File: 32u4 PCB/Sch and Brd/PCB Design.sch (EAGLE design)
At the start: 53 parts, among them J1 AVR_SPI_PROG_3X2PTH, J2 AMP FCI 10103594-0001LF, Q1 16MHz, U1 ATMEGA32U4-AU

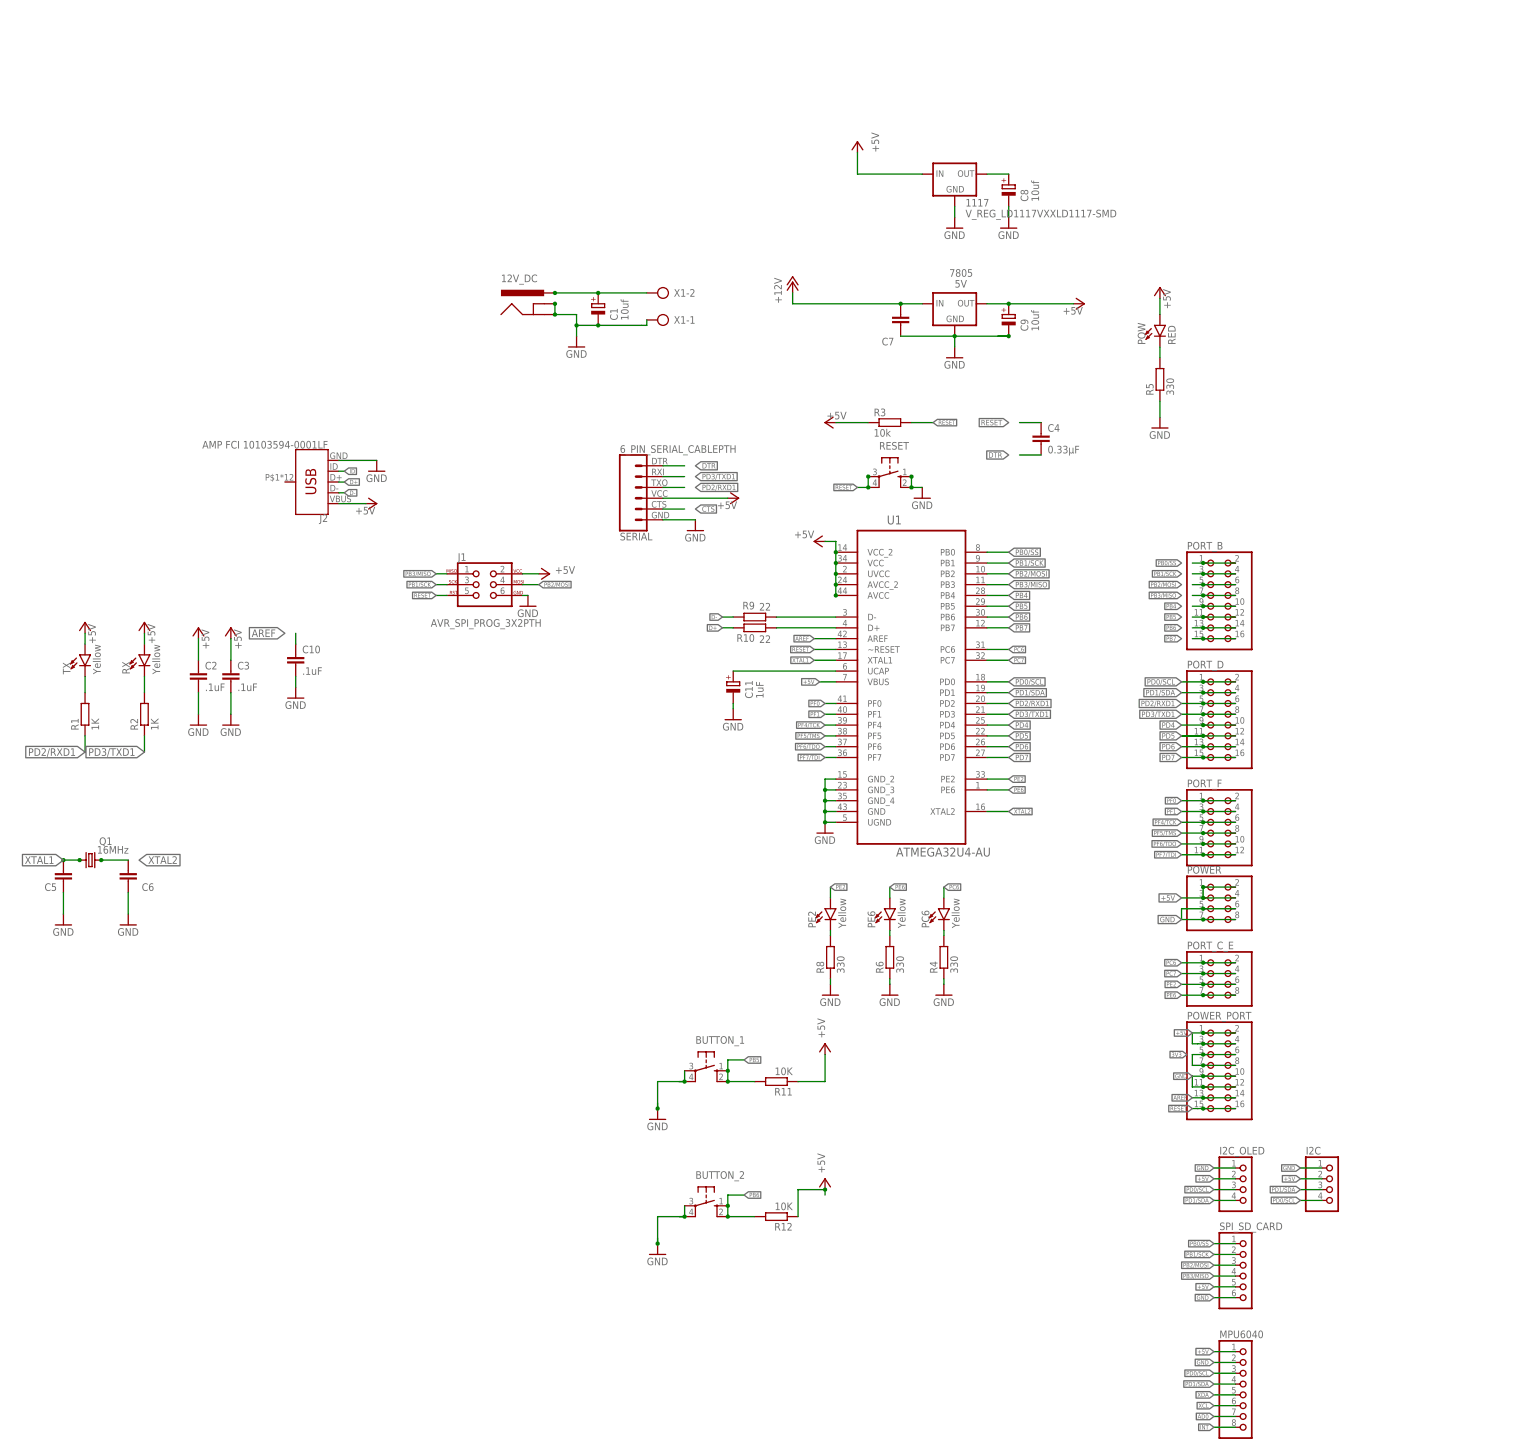
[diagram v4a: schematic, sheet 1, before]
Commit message: Adjusted Silkscreen, added bluetooth
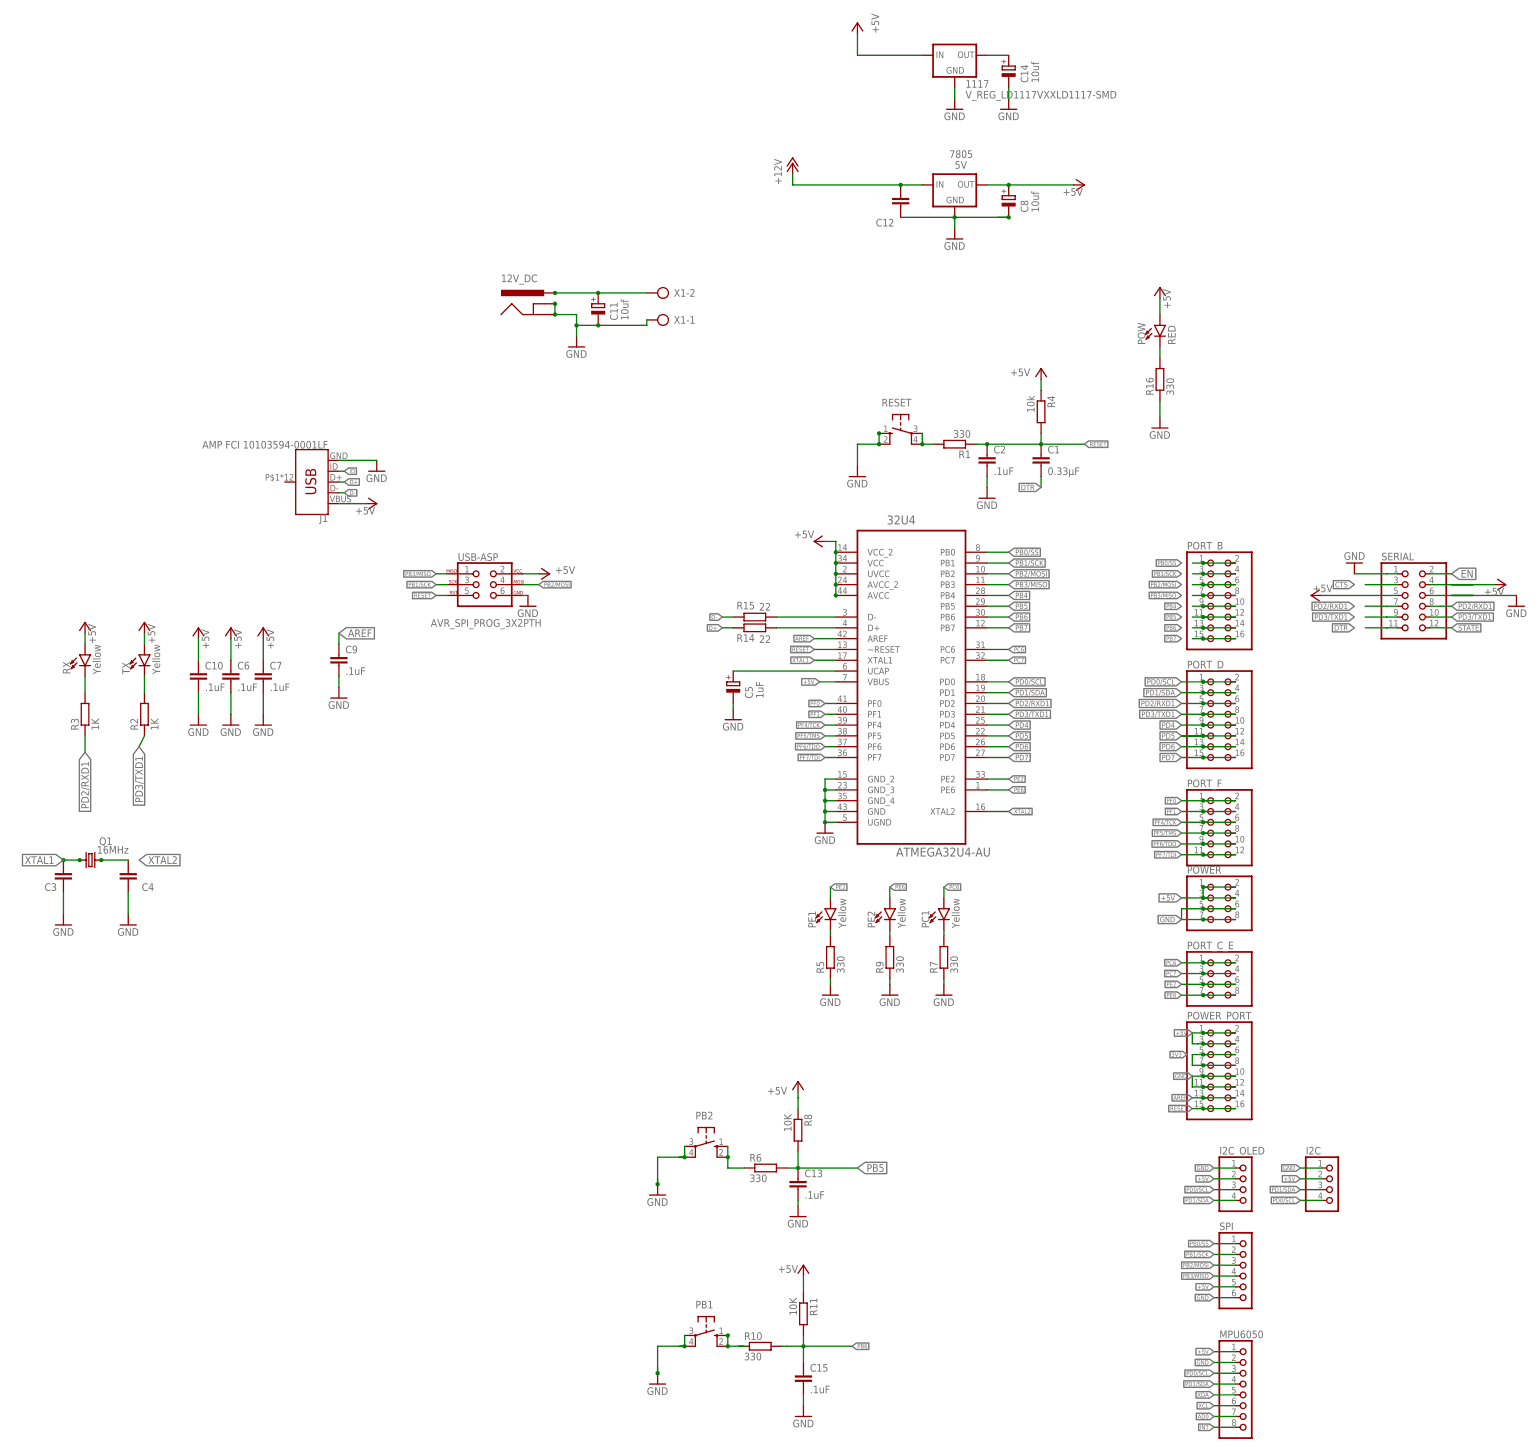
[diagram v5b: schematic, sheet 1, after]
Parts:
- removed BUTTON_1, BUTTON_2: (no value), switch-omron:10-XX
- removed J2: AMP FCI 10103594-0001LF, SparkFun-Connectors:USB_MICRO-B_HALF_PTH
- removed PE6: Yellow, SparkFun-LED:LED-BLUE0603
- added C12: .1uf, rcl:C-EUC0805K
- added C13, C15: .1uF, rcl:C-EUC0805K
- added C14: 10uf, resistor:CPOL-EUE2.5-6
- added PB1, PB2: (no value), switch-omron:10-XX
- added PE1: Yellow, SparkFun-LED:LED-BLUE0603
- added R14, R15: 22, resistor:R-EU_M0805
- added R16: 330, resistor:R-EU_M0805
- added USB-ASP: AVR_SPI_PROG_3X2PTH, SparkFun-Connectors:AVR_SPI_PROG_3X2PTH
- C1: value 10uf -> 0.33µF; device resistor:CPOL-EUE2.5-6 -> rcl:C-EUC0805K
- C11: value 1uF -> 10uf
- C3: value .1uF -> 22pF
- C4: value 0.33µF -> 22pF
- C5: value 22pF -> 1uF; device rcl:C-EUC0805K -> resistor:CPOL-EUE2.5-6
- C6: value 22pF -> .1uF
- C7: value .1uf -> .1uF
- C9: value 10uf -> .1uF; device resistor:CPOL-EUE2.5-6 -> rcl:C-EUC0805K
- J1: value AVR_SPI_PROG_3X2PTH -> AMP FCI 10103594-0001LF; device SparkFun-Connectors:AVR_SPI_PROG_3X2PTH -> SparkFun-Connectors:USB_MICRO-B_HALF_PTH; MF (none) -> AMPHENOL ICC (FCI); MPN (none) -> 10103594-0001LF; OC_FARNELL unknown -> 2293752
- R1: value 1K -> 330
- R10, R9: value 22 -> 330
- R12: value 10K -> 4k7
- R13: value 4k7 -> 220
- R3: value 10k -> 1K
- R4: value 330 -> 10k
- R7: value 220 -> 330
- R8: value 330 -> 10K
- SERIAL: value 6_PIN_SERIAL_CABLEPTH -> (none); device SparkFun-Connectors:6_PIN_SERIAL_CABLEPTH -> pinhead:PINHD-2X6; OC_FARNELL unknown -> (none)
- renumbered MPU6040 to MPU6050, PC6 to PC1, SPI_SD_CARD to SPI, U1 to 32U4
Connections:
- new net EN: SERIAL.2
- new net N$10: R1.2, RESET.P, RESET.P1
- new net N$11: PB1.S, PB1.S1, R10.1
- new net N$12: PB2.S, PB2.S1, R6.1
- new net STATE: SERIAL.12
- net +12V: now also C11.+, C12.1; no longer C1.+, C7.1
- net +5V: now also C10.1, C6.1, C7.1, C8.+, J1.VBUS, R4.1, R8.1, SERIAL.5, USB-ASP.2; no longer C2.1, C3.1, C9.+, J1.2, J2.VBUS, R12.1, R3.1
- net 3V3: now also C14.+; no longer C8.+
- net AREF: now also C9.1; no longer C10.1
- net CTS: now also SERIAL.3; no longer SERIAL.5
- net D+: now also J1.D+, R14.2; no longer J2.D+, R10.2
- net D-: now also J1.D-, R15.2; no longer J2.D-, R9.2
- net DTR: now also C1.2, SERIAL.11; no longer C4.2, SERIAL.1
- net GND: now also C12.2, C13.2, C14.-, C15.2, C3.1, C4.1, C5.-, C6.2, C9.2, J1.GND, PB1.P, PB1.P1, PB2.P, PB2.P1, R12.1, R16.1, R9.1, SERIAL.1, USB-ASP.6; no longer BUTTON_1.P, BUTTON_1.P1, BUTTON_2.P, BUTTON_2.P1, C1.-, C3.2, C5.1, C6.1, C9.-, J1.6, J2.GND, R4.1, R6.1, R8.1
- net ID: now also J1.ID; no longer J2.ID
- net N$1: now also R7.2; no longer R4.2
- net N$13: now also R15.1; no longer R9.1
- net N$14: now also R13.2; no longer R7.2
- net N$15: now also R14.1; no longer R10.1
- net N$16: now also C5.+; no longer C11.+
- net N$2: now also R16.2; no longer R5.2
- net N$3: now also PE2.C, R9.2; no longer PE6.C, R6.2
- net N$6: now also R12.2; no longer R13.2
- net N$7: now also PE1.C, R5.2; no longer PE2.C, R8.2
- net N$8: now also TX.C; no longer RX.C
- net N$9: now also R3.2, RX.C; no longer R1.2, TX.C
- net PB1/SCK: now also USB-ASP.3; no longer J1.3
- net PB2/MOSI: now also USB-ASP.4; no longer J1.4
- net PB3/MISO: now also USB-ASP.1; no longer J1.1
- net PB5: now also C13.1, R6.2, R8.2; no longer BUTTON_1.S, BUTTON_1.S1, R11.2
- net PB6: now also C15.1, R10.2, R11.2; no longer BUTTON_2.S, BUTTON_2.S1, R12.2
- net PD2/RXD1: now also R3.1, SERIAL.7, SERIAL.8; no longer R1.1, SERIAL.3
- net PD3/TXD1: now also SERIAL.10, SERIAL.9; no longer SERIAL.2
- net PE2: now also PE1.A; no longer PE2.A
- net PE6: now also PE2.A; no longer PE6.A
- net RESET: now also C1.1, C2.1, R1.1, R4.2, USB-ASP.5; no longer C4.1, J1.5, R3.2, RESET.P, RESET.P1
- net XTAL1: now also C3.2; no longer C5.2
- net XTAL2: now also C4.2; no longer C6.2
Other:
- moved on the sheet: 1117, 7805, C10, C11, C2, C3, C4, C6, C7, C8, PE2, R1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

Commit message: Manufacture
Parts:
- removed J1: AMP FCI 10103594-0001LF, SparkFun-Connectors:USB_MICRO-B_HALF_PTH
- added R17: 22, resistor:R-EU_M0805
- added R18: 330, resistor:R-EU_M0805
- added U1: (no value), MicroUSB:USB""
- 1117: value V_REG_LD1117VXXLD1117-SMD -> 3v3
- I2C: device pinhead:PINHD-1X4 -> pinhead:PINHD-2X4; OC_FARNELL unknown -> (none)
- R10: value 330 -> 10K
- R11, R8: value 10K -> 330
- R12: value 4k7 -> 330
- R13: value 220 -> 10K
- R14: value 22 -> 4k7
- R15: value 22 -> 220
- R16: value 330 -> 22
- R5, R6: value 330 -> I2C
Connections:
- removed net D+: J1.D+, R14.2
- removed net D-: J1.D-, R15.2
- removed net INT: MPU6050.8
- removed net N$13: 32U4.D-, R15.1
- removed net N$15: 32U4.D+, R14.1
- new net D_N: 32U4.D-, R17.1
- new net D_P: 32U4.D+, R16.1
- new net D_USB_N: R17.2, U1.D-
- new net D_USB_P: R16.2, U1.D+
- net +5V: now also I2C.3, I2C.4, R10.1, R13.1, R5.1, R6.1, U1.VBUS; no longer I2C.2, J1.VBUS, R11.1, R8.1
- net GND: now also I2C.2, R11.1, R14.1, R15.1, R18.1, U1.GND; no longer J1.GND, R12.1, R13.1, R16.1, R5.1
- net ID: now also U1.USBID; no longer J1.ID
- net N$1: now also R9.2; no longer R7.2
- net N$11: now also R12.1; no longer R10.1
- net N$12: now also R8.1; no longer R6.1
- net N$14: now also R15.2; no longer R13.2
- net N$2: now also R18.2; no longer R16.2
- net N$3: now also R11.2; no longer R9.2
- net N$6: now also R14.2; no longer R12.2
- net N$7: now also R7.2; no longer R5.2
- net PB4: now also MPU6050.8
- net PB5: now also R10.2; no longer R6.2
- net PB6: now also R12.2, R13.2; no longer R10.2, R11.2
- net PD0/SCL: now also I2C.7, I2C.8, R5.2; no longer I2C.4
- net PD1/SDA: now also I2C.5, I2C.6, R6.2; no longer I2C.3

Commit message: Changed values and modified BOM
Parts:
- R11, R18, R7, R9: value 330 -> 1k
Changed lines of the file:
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@@
 </part>
 <part name="GND15" library="supply1" deviceset="GND" device=""/>
-<part name="R9" library="resistor" library_urn="urn:adsk.eagle:library:348" deviceset="R-EU_" device="M0805" value="330">
+<part name="R9" library="resistor" library_urn="urn:adsk.eagle:library:348" deviceset="R-EU_" device="M0805" value="1k">
 <attribute name="MF" value=""/>
 <attribute name="MPN" value=""/>
@@
 <attribute name="OC_FARNELL" value="unknown"/>
 </part>
-<part name="R18" library="resistor" library_urn="urn:adsk.eagle:library:348" deviceset="R-EU_" device="M0805" value="330">
+<part name="R18" library="resistor" library_urn="urn:adsk.eagle:library:348" deviceset="R-EU_" device="M0805" value="1k">
 <attribute name="MF" value=""/>
 <attribute name="MPN" value=""/>
@@
 </part>
 <part name="GND2" library="supply1" deviceset="GND" device=""/>
-<part name="R11" library="resistor" library_urn="urn:adsk.eagle:library:348" deviceset="R-EU_" device="M0805" value="330">
+<part name="R11" library="resistor" library_urn="urn:adsk.eagle:library:348" deviceset="R-EU_" device="M0805" value="1k">
 <attribute name="MF" value=""/>
 <attribute name="MPN" value=""/>
@@
 </part>
 <part name="GND9" library="supply1" deviceset="GND" device=""/>
-<part name="R7" library="resistor" library_urn="urn:adsk.eagle:library:348" deviceset="R-EU_" device="M0805" value="330">
+<part name="R7" library="resistor" library_urn="urn:adsk.eagle:library:348" deviceset="R-EU_" device="M0805" value="1k">
 <attribute name="MF" value=""/>
 <attribute name="MPN" value=""/>

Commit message: Changed Silkscreen
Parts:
- removed PE1: Yellow, SparkFun-LED:LED-BLUE0603
- added PE6: Blue, SparkFun-LED:LED-BLUE0603
- PC6, PE2: value Yellow -> Blue
- renumbered PC1 to PC6
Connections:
- net N$3: now also PE6.C; no longer PE2.C
- net N$7: now also PE2.C; no longer PE1.C
- net PE2: now also PE2.A; no longer PE1.A
- net PE6: now also PE6.A; no longer PE2.A
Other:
- moved on the sheet: C10, C3, C4, C6, C7, PE2, Q1, R2, R3, RX, TX
